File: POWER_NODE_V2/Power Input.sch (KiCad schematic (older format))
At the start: 0 parts

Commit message: Schematic for Power Node V2 mostly done - mostly need connectors
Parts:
- added D? (x2): EL-17-21VGC/TR8, symbol LED
- added D? (x2): AS4PM-M3/86A, symbol D_ALT
- added J? (x4): CONN_01X02, symbol CONN_01X02
- added R? (x2): 2.2K / 0.1W / 1% / SMD 0603, symbol R
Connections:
- net labels added: +24V, GND
- wire segments 0 -> 13
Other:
- note added: "24V Power Input"
- note added: "DC BUS A"
- note added: "DC BUS B"
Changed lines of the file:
@@
 $Descr A4 11693 8268
 encoding utf-8
-Sheet 2 8
+Sheet 2 9
 Title ""
 Date ""
@@
 Comment4 ""
 $EndDescr
+Text Notes 7100 6950 0    197  ~ 0
+24V Power Input
+$Comp
+L CONN_01X02 J?
+U 1 1 59521C63
+P 4400 2450
+F 0 "J?" H 4400 2600 50  0000 C CNN
+F 1 "CONN_01X02" V 4500 2450 50  0000 C CNN
+F 2 "" H 4400 2450 50  0001 C CNN
+F 3 "" H 4400 2450 50  0001 C CNN
+	1    4400 2450
+	-1   0    0    1
+$EndComp
+$Comp
+L CONN_01X02 J?
+U 1 1 59521CC9
+P 5200 2200
+F 0 "J?" H 5200 2350 50  0000 C CNN
+F 1 "CONN_01X02" V 5300 2200 50  0000 C CNN
+F 2 "" H 5200 2200 50  0001 C CNN
+F 3 "" H 5200 2200 50  0001 C CNN
+	1    5200 2200
+	0    -1   -1   0
+$EndComp
+$Comp
+L R R?
+U 1 1 59521D14
+P 5950 2750
+F 0 "R?" H 6100 2700 50  0000 C CNN
+F 1 "2.2K / 0.1W / 1% / SMD 0603" H 6650 2800 50  0000 C CNN
+F 2 "" V 5880 2750 50  0001 C CNN
+F 3 "" H 5950 2750 50  0001 C CNN
+	1    5950 2750
+	1    0    0    -1
+$EndComp
+$Comp
+L LED D?
+U 1 1 59522073
+P 5950 3150
+F 0 "D?" V 5900 3000 50  0000 C CNN
+F 1 "EL-17-21VGC/TR8" V 6000 2650 50  0000 C CNN
+F 2 "" H 5950 3150 50  0001 C CNN
+F 3 "" H 5950 3150 50  0001 C CNN
+	1    5950 3150
+	0    -1   -1   0
+$EndComp
+$Comp
+L D_ALT D?
+U 1 1 595220C4
+P 6500 2400
+F 0 "D?" H 6500 2500 50  0000 C CNN
+F 1 "AS4PM-M3/86A" H 6500 2300 50  0000 C CNN
+F 2 "" H 6500 2400 50  0001 C CNN
+F 3 "" H 6500 2400 50  0001 C CNN
+	1    6500 2400
+	-1   0    0    1
+$EndComp
+Wire Wire Line
+	5950 2600 5950 2400
+Wire Wire Line
+	5250 2400 6350 2400
+Wire Wire Line
+	5950 2900 5950 3000
+Wire Wire Line
+	4600 2400 5150 2400
+Connection ~ 5950 2400
+$Comp
+L GND #PWR?
+U 1 1 5952286D
+P 5950 3450
+F 0 "#PWR?" H 5950 3200 50  0001 C CNN
+F 1 "GND" H 5950 3300 50  0000 C CNN
+F 2 "" H 5950 3450 50  0001 C CNN
+F 3 "" H 5950 3450 50  0001 C CNN
+	1    5950 3450
+	1    0    0    -1
+$EndComp
+Wire Wire Line
+	5950 3450 5950 3300
+Text Notes 3250 2550 0    118  ~ 0
+DC BUS A
+$Comp
+L CONN_01X02 J?
+U 1 1 59522A4E
+P 4400 4150
+F 0 "J?" H 4400 4300 50  0000 C CNN
+F 1 "CONN_01X02" V 4500 4150 50  0000 C CNN
+F 2 "" H 4400 4150 50  0001 C CNN
+F 3 "" H 4400 4150 50  0001 C CNN
+	1    4400 4150
+	-1   0    0    1
+$EndComp
+$Comp
+L CONN_01X02 J?
+U 1 1 59522A54
+P 5200 3900
+F 0 "J?" H 5200 4050 50  0000 C CNN
+F 1 "CONN_01X02" V 5300 3900 50  0000 C CNN
+F 2 "" H 5200 3900 50  0001 C CNN
+F 3 "" H 5200 3900 50  0001 C CNN
+	1    5200 3900
+	0    -1   -1   0
+$EndComp
+$Comp
+L R R?
+U 1 1 59522A5A
+P 5950 4450
+F 0 "R?" H 6100 4400 50  0000 C CNN
+F 1 "2.2K / 0.1W / 1% / SMD 0603" H 6650 4500 50  0000 C CNN
+F 2 "" V 5880 4450 50  0001 C CNN
+F 3 "" H 5950 4450 50  0001 C CNN
+	1    5950 4450
+	1    0    0    -1
+$EndComp
+$Comp
+L LED D?
+U 1 1 59522A60
+P 5950 4850
+F 0 "D?" V 5900 4700 50  0000 C CNN
+F 1 "EL-17-21VGC/TR8" V 6000 4350 50  0000 C CNN
+F 2 "" H 5950 4850 50  0001 C CNN
+F 3 "" H 5950 4850 50  0001 C CNN
+	1    5950 4850
+	0    -1   -1   0
+$EndComp
+$Comp
+L D_ALT D?
+U 1 1 59522A66
+P 6500 4100
+F 0 "D?" H 6500 4200 50  0000 C CNN
+F 1 "AS4PM-M3/86A" H 6500 4000 50  0000 C CNN
+F 2 "" H 6500 4100 50  0001 C CNN
+F 3 "" H 6500 4100 50  0001 C CNN
+	1    6500 4100
+	-1   0    0    1
+$EndComp
+Wire Wire Line
+	5950 4300 5950 4100
+Wire Wire Line
+	5250 4100 6350 4100
+Wire Wire Line
+	5950 4600 5950 4700
+Wire Wire Line
+	4600 4100 5150 4100
+Connection ~ 5950 4100
+$Comp
+L GND #PWR?
+U 1 1 59522A7A
+P 5950 5150
+F 0 "#PWR?" H 5950 4900 50  0001 C CNN
+F 1 "GND" H 5950 5000 50  0000 C CNN
+F 2 "" H 5950 5150 50  0001 C CNN
+F 3 "" H 5950 5150 50  0001 C CNN
+	1    5950 5150
+	1    0    0    -1
+$EndComp
+Wire Wire Line
+	5950 5150 5950 5000
+Wire Wire Line
+	6650 2400 7850 2400
+Wire Wire Line
+	7850 2000 7850 4100
+Wire Wire Line
+	7850 4100 6650 4100
+$Comp
+L +24V #PWR?
+U 1 1 59522AEA
+P 7850 2000
+F 0 "#PWR?" H 7850 1850 50  0001 C CNN
+F 1 "+24V" H 7850 2140 50  0000 C CNN
+F 2 "" H 7850 2000 50  0001 C CNN
+F 3 "" H 7850 2000 50  0001 C CNN
+	1    7850 2000
+	1    0    0    -1
+$EndComp
+Connection ~ 7850 2400
+Text Notes 3250 4200 0    118  ~ 0
+DC BUS B
 $EndSCHEMATC

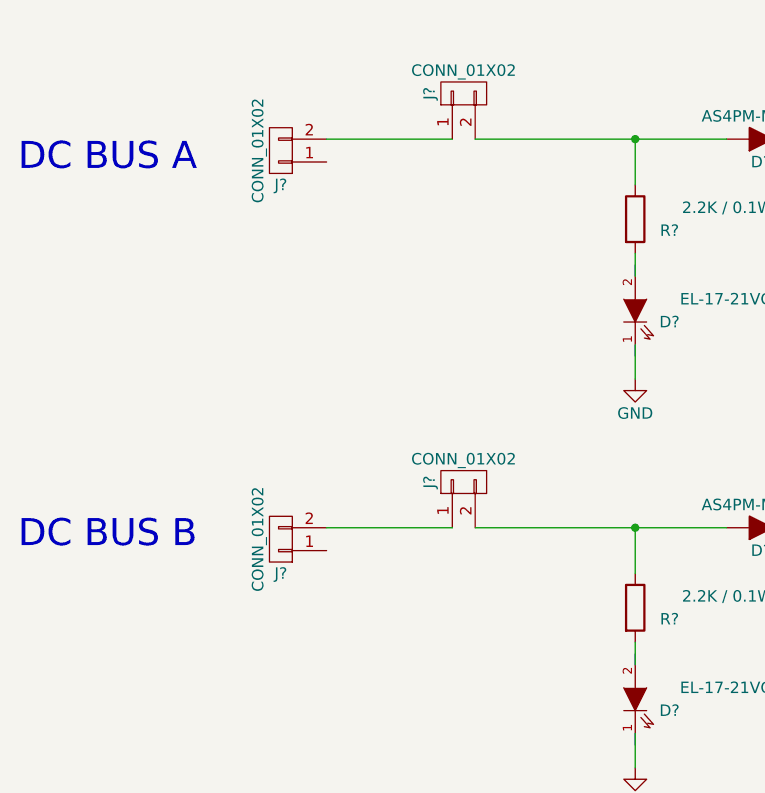
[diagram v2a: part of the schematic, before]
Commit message: Add Gnd to power inputs
oops.
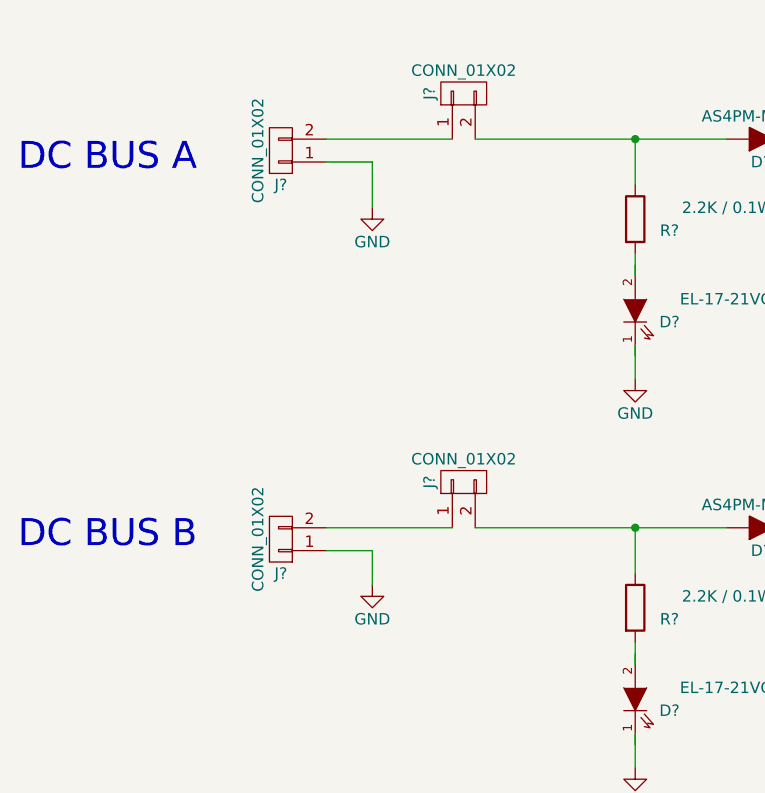
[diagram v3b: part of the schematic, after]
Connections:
- wire segments 13 -> 17
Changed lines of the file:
@@
 Text Notes 3250 4200 0    118  ~ 0
 DC BUS B
+$Comp
+L GND #PWR?
+U 1 1 5952F227
+P 4800 2700
+F 0 "#PWR?" H 4800 2450 50  0001 C CNN
+F 1 "GND" H 4800 2550 50  0000 C CNN
+F 2 "" H 4800 2700 50  0001 C CNN
+F 3 "" H 4800 2700 50  0001 C CNN
+	1    4800 2700
+	1    0    0    -1
+$EndComp
+Wire Wire Line
+	4800 2700 4800 2500
+Wire Wire Line
+	4800 2500 4600 2500
+$Comp
+L GND #PWR?
+U 1 1 5952F2BA
+P 4800 4350
+F 0 "#PWR?" H 4800 4100 50  0001 C CNN
+F 1 "GND" H 4800 4200 50  0000 C CNN
+F 2 "" H 4800 4350 50  0001 C CNN
+F 3 "" H 4800 4350 50  0001 C CNN
+	1    4800 4350
+	1    0    0    -1
+$EndComp
+Wire Wire Line
+	4800 4350 4800 4200
+Wire Wire Line
+	4800 4200 4600 4200
 $EndSCHEMATC

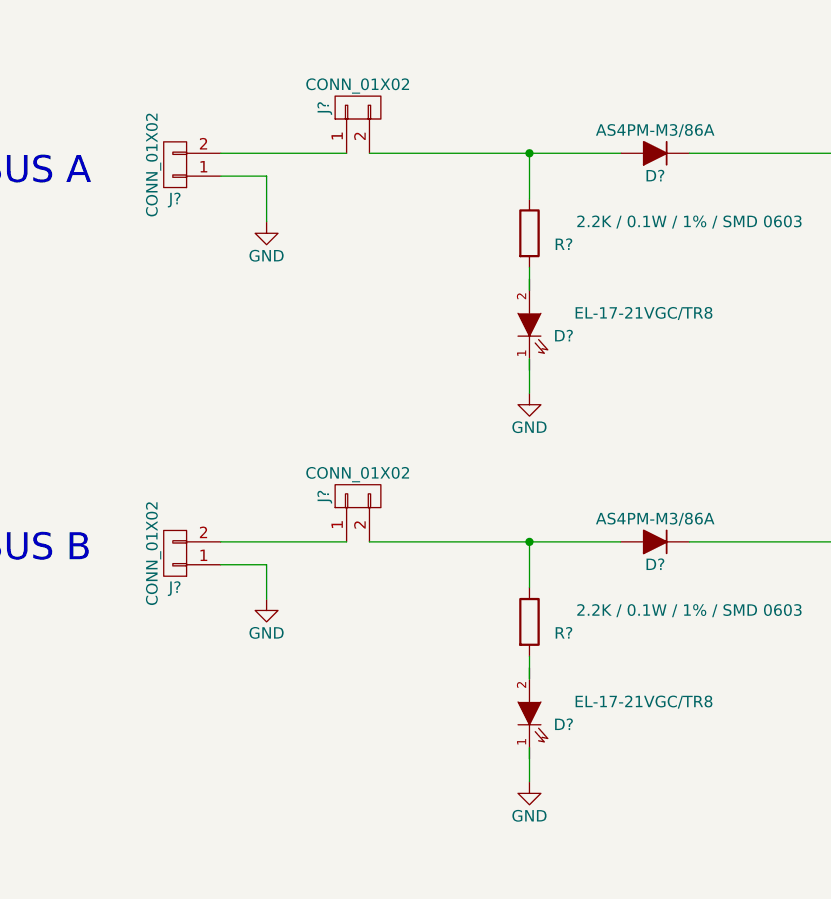
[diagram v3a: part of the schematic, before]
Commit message: made a lot of footprints, began PCB layout for power node v2
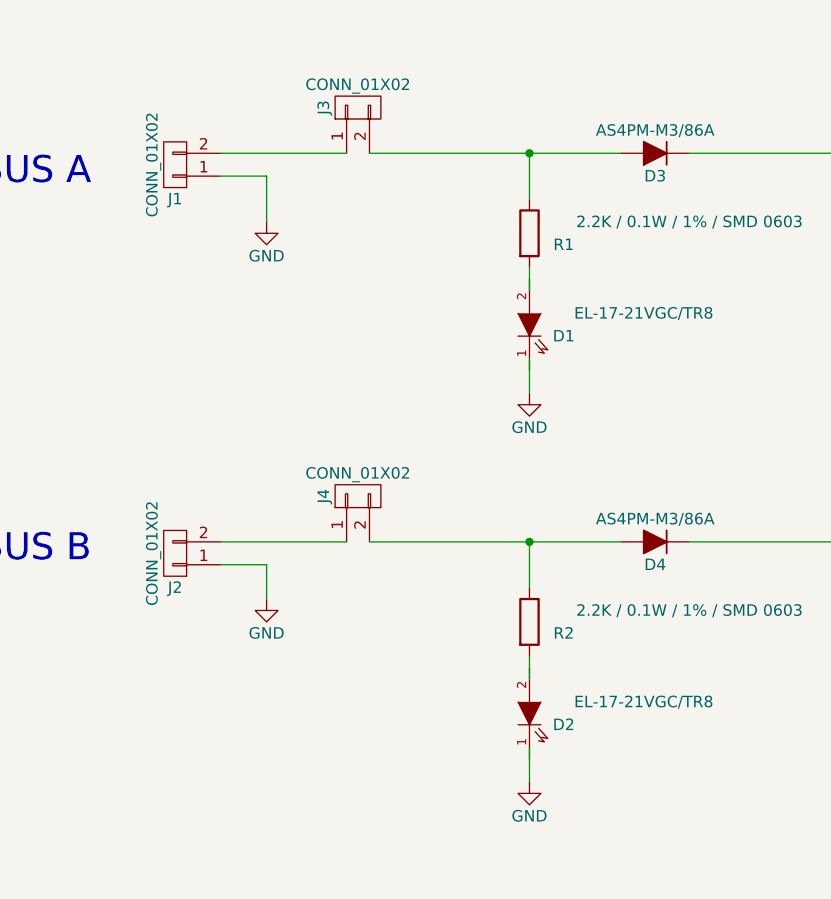
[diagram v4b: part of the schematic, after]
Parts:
- D1, D2: renamed from D?; footprint (none) -> rLoop Footprints:LED_0805
- D3, D4: renamed from D?; footprint (none) -> rLoop Footprints:TO-277A_SMPC
- J1, J2, J3, J4: renamed from J?; footprint (none) -> Pin_Headers:Pin_Header_Straight_1x02_Pitch2.54mm
- R1, R2: renamed from R?; footprint (none) -> Resistors_SMD:R_0603
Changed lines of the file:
@@
 24V Power Input
 $Comp
-L CONN_01X02 J?
+L CONN_01X02 J1
 U 1 1 59521C63
 P 4400 2450
-F 0 "J?" H 4400 2600 50  0000 C CNN
+F 0 "J1" H 4400 2600 50  0000 C CNN
 F 1 "CONN_01X02" V 4500 2450 50  0000 C CNN
-F 2 "" H 4400 2450 50  0001 C CNN
+F 2 "Pin_Headers:Pin_Header_Straight_1x02_Pitch2.54mm" H 4400 2450 50  0001 C CNN
 F 3 "" H 4400 2450 50  0001 C CNN
 	1    4400 2450
@@
 $EndComp
 $Comp
-L CONN_01X02 J?
+L CONN_01X02 J3
 U 1 1 59521CC9
 P 5200 2200
-F 0 "J?" H 5200 2350 50  0000 C CNN
+F 0 "J3" H 5200 2350 50  0000 C CNN
 F 1 "CONN_01X02" V 5300 2200 50  0000 C CNN
-F 2 "" H 5200 2200 50  0001 C CNN
+F 2 "Pin_Headers:Pin_Header_Straight_1x02_Pitch2.54mm" H 5200 2200 50  0001 C CNN
 F 3 "" H 5200 2200 50  0001 C CNN
 	1    5200 2200
@@
 $EndComp
 $Comp
-L R R?
+L R R1
 U 1 1 59521D14
 P 5950 2750
-F 0 "R?" H 6100 2700 50  0000 C CNN
+F 0 "R1" H 6100 2700 50  0000 C CNN
 F 1 "2.2K / 0.1W / 1% / SMD 0603" H 6650 2800 50  0000 C CNN
-F 2 "" V 5880 2750 50  0001 C CNN
+F 2 "Resistors_SMD:R_0603" V 5880 2750 50  0001 C CNN
 F 3 "" H 5950 2750 50  0001 C CNN
 	1    5950 2750
@@
 $EndComp
 $Comp
-L LED D?
-U 1 1 59522073
-P 5950 3150
-F 0 "D?" V 5900 3000 50  0000 C CNN
-F 1 "EL-17-21VGC/TR8" V 6000 2650 50  0000 C CNN
-F 2 "" H 5950 3150 50  0001 C CNN
-F 3 "" H 5950 3150 50  0001 C CNN
-	1    5950 3150
-	0    -1   -1   0
-$EndComp
-$Comp
-L D_ALT D?
+L D_ALT D3
 U 1 1 595220C4
 P 6500 2400
-F 0 "D?" H 6500 2500 50  0000 C CNN
+F 0 "D3" H 6500 2500 50  0000 C CNN
 F 1 "AS4PM-M3/86A" H 6500 2300 50  0000 C CNN
-F 2 "" H 6500 2400 50  0001 C CNN
+F 2 "rLoop Footprints:TO-277A_SMPC" H 6500 2400 50  0001 C CNN
 F 3 "" H 6500 2400 50  0001 C CNN
 	1    6500 2400
@@
 Connection ~ 5950 2400
 $Comp
-L GND #PWR?
+L GND #PWR01
 U 1 1 5952286D
 P 5950 3450
-F 0 "#PWR?" H 5950 3200 50  0001 C CNN
+F 0 "#PWR01" H 5950 3200 50  0001 C CNN
 F 1 "GND" H 5950 3300 50  0000 C CNN
 F 2 "" H 5950 3450 50  0001 C CNN
@@
 DC BUS A
 $Comp
-L CONN_01X02 J?
+L CONN_01X02 J2
 U 1 1 59522A4E
 P 4400 4150
-F 0 "J?" H 4400 4300 50  0000 C CNN
+F 0 "J2" H 4400 4300 50  0000 C CNN
 F 1 "CONN_01X02" V 4500 4150 50  0000 C CNN
-F 2 "" H 4400 4150 50  0001 C CNN
+F 2 "Pin_Headers:Pin_Header_Straight_1x02_Pitch2.54mm" H 4400 4150 50  0001 C CNN
 F 3 "" H 4400 4150 50  0001 C CNN
 	1    4400 4150
@@
 $EndComp
 $Comp
-L CONN_01X02 J?
+L CONN_01X02 J4
 U 1 1 59522A54
 P 5200 3900
-F 0 "J?" H 5200 4050 50  0000 C CNN
+F 0 "J4" H 5200 4050 50  0000 C CNN
 F 1 "CONN_01X02" V 5300 3900 50  0000 C CNN
-F 2 "" H 5200 3900 50  0001 C CNN
+F 2 "Pin_Headers:Pin_Header_Straight_1x02_Pitch2.54mm" H 5200 3900 50  0001 C CNN
 F 3 "" H 5200 3900 50  0001 C CNN
 	1    5200 3900
@@
 $EndComp
 $Comp
-L R R?
+L R R2
 U 1 1 59522A5A
 P 5950 4450
-F 0 "R?" H 6100 4400 50  0000 C CNN
+F 0 "R2" H 6100 4400 50  0000 C CNN
 F 1 "2.2K / 0.1W / 1% / SMD 0603" H 6650 4500 50  0000 C CNN
-F 2 "" V 5880 4450 50  0001 C CNN
+F 2 "Resistors_SMD:R_0603" V 5880 4450 50  0001 C CNN
 F 3 "" H 5950 4450 50  0001 C CNN
 	1    5950 4450
@@
 $EndComp
 $Comp
-L LED D?
-U 1 1 59522A60
-P 5950 4850
-F 0 "D?" V 5900 4700 50  0000 C CNN
-F 1 "EL-17-21VGC/TR8" V 6000 4350 50  0000 C CNN
-F 2 "" H 5950 4850 50  0001 C CNN
-F 3 "" H 5950 4850 50  0001 C CNN
-	1    5950 4850
-	0    -1   -1   0
-$EndComp
-$Comp
-L D_ALT D?
+L D_ALT D4
 U 1 1 59522A66
 P 6500 4100
-F 0 "D?" H 6500 4200 50  0000 C CNN
+F 0 "D4" H 6500 4200 50  0000 C CNN
 F 1 "AS4PM-M3/86A" H 6500 4000 50  0000 C CNN
-F 2 "" H 6500 4100 50  0001 C CNN
+F 2 "rLoop Footprints:TO-277A_SMPC" H 6500 4100 50  0001 C CNN
 F 3 "" H 6500 4100 50  0001 C CNN
 	1    6500 4100
@@
 Connection ~ 5950 4100
 $Comp
-L GND #PWR?
+L GND #PWR02
 U 1 1 59522A7A
 P 5950 5150
-F 0 "#PWR?" H 5950 4900 50  0001 C CNN
+F 0 "#PWR02" H 5950 4900 50  0001 C CNN
 F 1 "GND" H 5950 5000 50  0000 C CNN
 F 2 "" H 5950 5150 50  0001 C CNN
@@
 	7850 4100 6650 4100
 $Comp
-L +24V #PWR?
+L +24V #PWR03
 U 1 1 59522AEA
 P 7850 2000
-F 0 "#PWR?" H 7850 1850 50  0001 C CNN
+F 0 "#PWR03" H 7850 1850 50  0001 C CNN
 F 1 "+24V" H 7850 2140 50  0000 C CNN
 F 2 "" H 7850 2000 50  0001 C CNN
@@
 DC BUS B
 $Comp
-L GND #PWR?
+L GND #PWR04
 U 1 1 5952F227
 P 4800 2700
-F 0 "#PWR?" H 4800 2450 50  0001 C CNN
+F 0 "#PWR04" H 4800 2450 50  0001 C CNN
 F 1 "GND" H 4800 2550 50  0000 C CNN
 F 2 "" H 4800 2700 50  0001 C CNN
@@
 	4800 2500 4600 2500
 $Comp
-L GND #PWR?
+L GND #PWR05
 U 1 1 5952F2BA
 P 4800 4350
-F 0 "#PWR?" H 4800 4100 50  0001 C CNN
+F 0 "#PWR05" H 4800 4100 50  0001 C CNN
 F 1 "GND" H 4800 4200 50  0000 C CNN
 F 2 "" H 4800 4350 50  0001 C CNN
@@
 Wire Wire Line
 	4800 4200 4600 4200
+$Comp
+L LED D2
+U 1 1 59522A60
+P 5950 4850
+F 0 "D2" V 5900 4700 50  0000 C CNN
+F 1 "EL-17-21VGC/TR8" V 6000 4350 50  0000 C CNN
+F 2 "rLoop Footprints:LED_0805" H 5950 4850 50  0001 C CNN
+F 3 "" H 5950 4850 50  0001 C CNN
+	1    5950 4850
+	0    -1   -1   0
+$EndComp
+$Comp
+L LED D1
+U 1 1 59522073
+P 5950 3150
+F 0 "D1" V 5900 3000 50  0000 C CNN
+F 1 "EL-17-21VGC/TR8" V 6000 2650 50  0000 C CNN
+F 2 "rLoop Footprints:LED_0805" H 5950 3150 50  0001 C CNN
+F 3 "" H 5950 3150 50  0001 C CNN
+	1    5950 3150
+	0    -1   -1   0
+$EndComp
 $EndSCHEMATC

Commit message: Power Node v2 WIP
TODO: 3d models, double check everything, update connector P/N on
schematics, align boards and drill holes
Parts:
- J1, J2: footprint Pin_Headers:Pin_Header_Straight_1x02_Pitch2.54mm -> rLoop Footprints:TE_1744055-2_3.96_EP_HDR_ASSY_2P_VERT_HT
- J3, J4: footprint Pin_Headers:Pin_Header_Straight_1x02_Pitch2.54mm -> rLoop Footprints:Keystone_3544-2
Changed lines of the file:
@@
 F 0 "J1" H 4400 2600 50  0000 C CNN
 F 1 "CONN_01X02" V 4500 2450 50  0000 C CNN
-F 2 "Pin_Headers:Pin_Header_Straight_1x02_Pitch2.54mm" H 4400 2450 50  0001 C CNN
+F 2 "rLoop Footprints:TE_1744055-2_3.96_EP_HDR_ASSY_2P_VERT_HT" H 4400 2450 50  0001 C CNN
 F 3 "" H 4400 2450 50  0001 C CNN
 	1    4400 2450
@@
 F 0 "J3" H 5200 2350 50  0000 C CNN
 F 1 "CONN_01X02" V 5300 2200 50  0000 C CNN
-F 2 "Pin_Headers:Pin_Header_Straight_1x02_Pitch2.54mm" H 5200 2200 50  0001 C CNN
+F 2 "rLoop Footprints:Keystone_3544-2" H 5200 2200 50  0001 C CNN
 F 3 "" H 5200 2200 50  0001 C CNN
 	1    5200 2200
@@
 F 0 "J2" H 4400 4300 50  0000 C CNN
 F 1 "CONN_01X02" V 4500 4150 50  0000 C CNN
-F 2 "Pin_Headers:Pin_Header_Straight_1x02_Pitch2.54mm" H 4400 4150 50  0001 C CNN
+F 2 "rLoop Footprints:TE_1744055-2_3.96_EP_HDR_ASSY_2P_VERT_HT" H 4400 4150 50  0001 C CNN
 F 3 "" H 4400 4150 50  0001 C CNN
 	1    4400 4150
@@
 F 0 "J4" H 5200 4050 50  0000 C CNN
 F 1 "CONN_01X02" V 5300 3900 50  0000 C CNN
-F 2 "Pin_Headers:Pin_Header_Straight_1x02_Pitch2.54mm" H 5200 3900 50  0001 C CNN
+F 2 "rLoop Footprints:Keystone_3544-2" H 5200 3900 50  0001 C CNN
 F 3 "" H 5200 3900 50  0001 C CNN
 	1    5200 3900

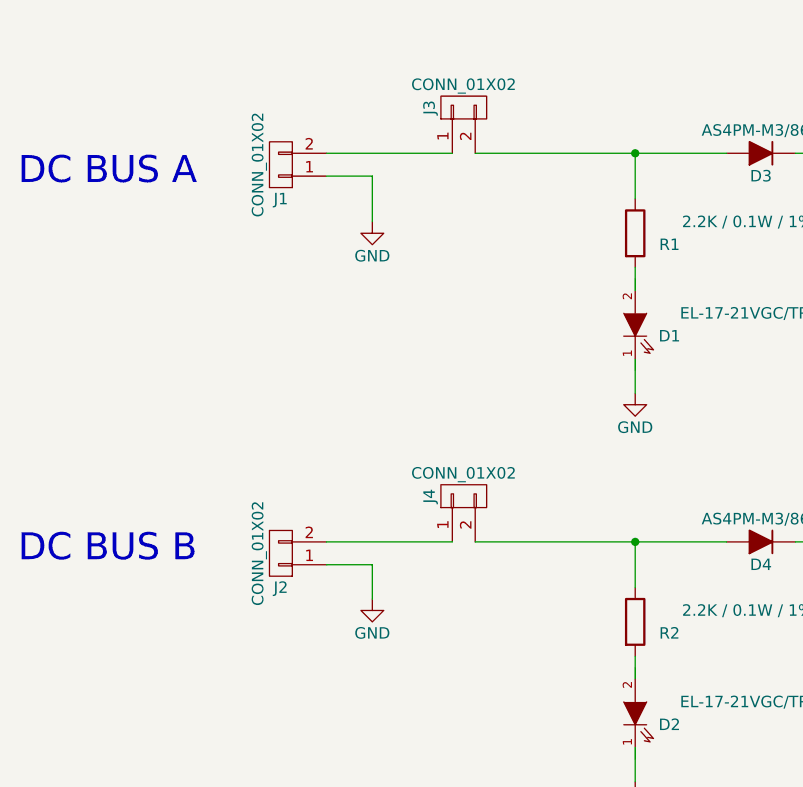
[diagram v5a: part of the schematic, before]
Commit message: 3d model work
TODO: change 2 pins to MTA156
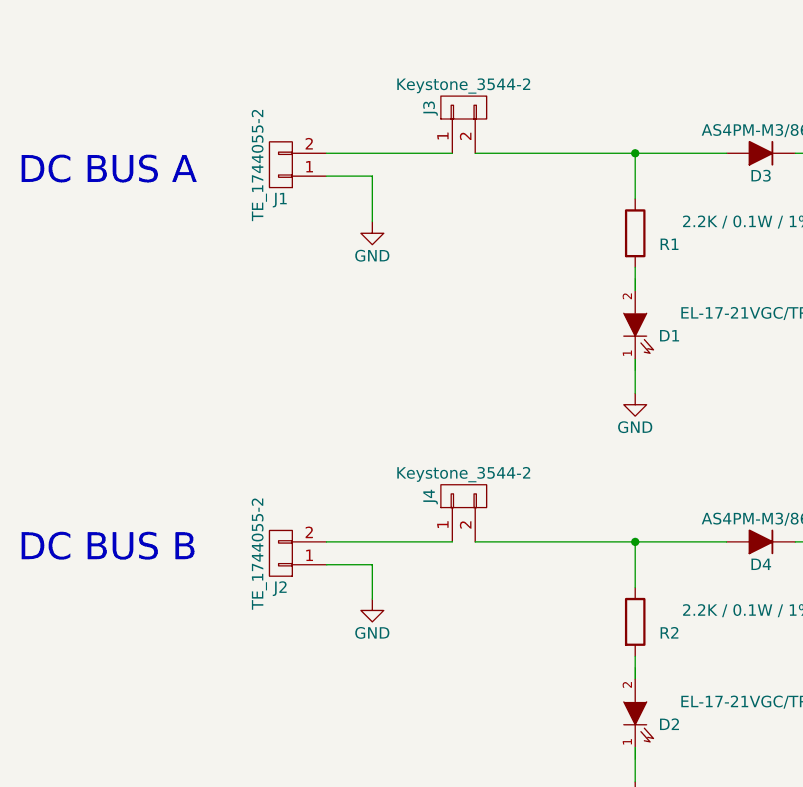
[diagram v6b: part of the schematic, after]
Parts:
- J1, J2: value CONN_01X02 -> TE_1744055-2
- J3, J4: value CONN_01X02 -> Keystone_3544-2
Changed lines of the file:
@@
 P 4400 2450
 F 0 "J1" H 4400 2600 50  0000 C CNN
-F 1 "CONN_01X02" V 4500 2450 50  0000 C CNN
+F 1 "TE_1744055-2" V 4500 2450 50  0000 C CNN
 F 2 "rLoop Footprints:TE_1744055-2_3.96_EP_HDR_ASSY_2P_VERT_HT" H 4400 2450 50  0001 C CNN
 F 3 "" H 4400 2450 50  0001 C CNN
@@
 P 5200 2200
 F 0 "J3" H 5200 2350 50  0000 C CNN
-F 1 "CONN_01X02" V 5300 2200 50  0000 C CNN
+F 1 "Keystone_3544-2" V 5300 2200 50  0000 C CNN
 F 2 "rLoop Footprints:Keystone_3544-2" H 5200 2200 50  0001 C CNN
 F 3 "" H 5200 2200 50  0001 C CNN
@@
 P 4400 4150
 F 0 "J2" H 4400 4300 50  0000 C CNN
-F 1 "CONN_01X02" V 4500 4150 50  0000 C CNN
+F 1 "TE_1744055-2" V 4500 4150 50  0000 C CNN
 F 2 "rLoop Footprints:TE_1744055-2_3.96_EP_HDR_ASSY_2P_VERT_HT" H 4400 4150 50  0001 C CNN
 F 3 "" H 4400 4150 50  0001 C CNN
@@
 P 5200 3900
 F 0 "J4" H 5200 4050 50  0000 C CNN
-F 1 "CONN_01X02" V 5300 3900 50  0000 C CNN
+F 1 "Keystone_3544-2" V 5300 3900 50  0000 C CNN
 F 2 "rLoop Footprints:Keystone_3544-2" H 5200 3900 50  0001 C CNN
 F 3 "" H 5200 3900 50  0001 C CNN
